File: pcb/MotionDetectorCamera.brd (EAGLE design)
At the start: 55.9 x 44.5 mm, 134 parts, among them J2 S-MOUNT-LENS-HOLDER, J3 MINI-USB-JACK, U1 LATTICE-ICE40HX4K-BG121, U10 NXP-NTB0102, U11 ON-NLAS3157, U12 ON-NLAS3157, U13 STM-STM32F730, U2 TI-TPS6280XYKAR, U22 TI-TPD4S012DRYR, U3 MICROSD-SOCKET, U4 TI-TPS6280XYKAR, U5 W989D6DBGX6I, U6 TI-TPS63805YFFR, U8 ON-AR0330CS1C12SPKA0, U9 TI-TMUX1574, X1 SITIME-SIT8021, X2 SITIME-SIT8021

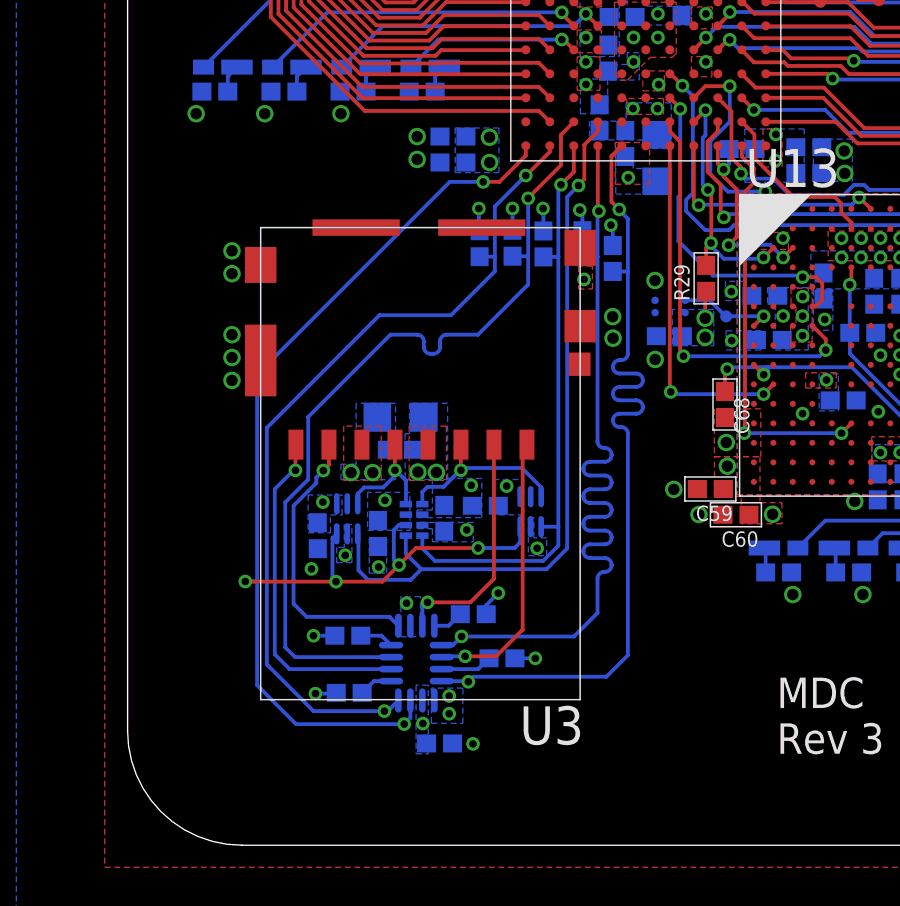
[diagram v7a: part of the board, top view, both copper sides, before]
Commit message: In process of length-matching SDIO lines
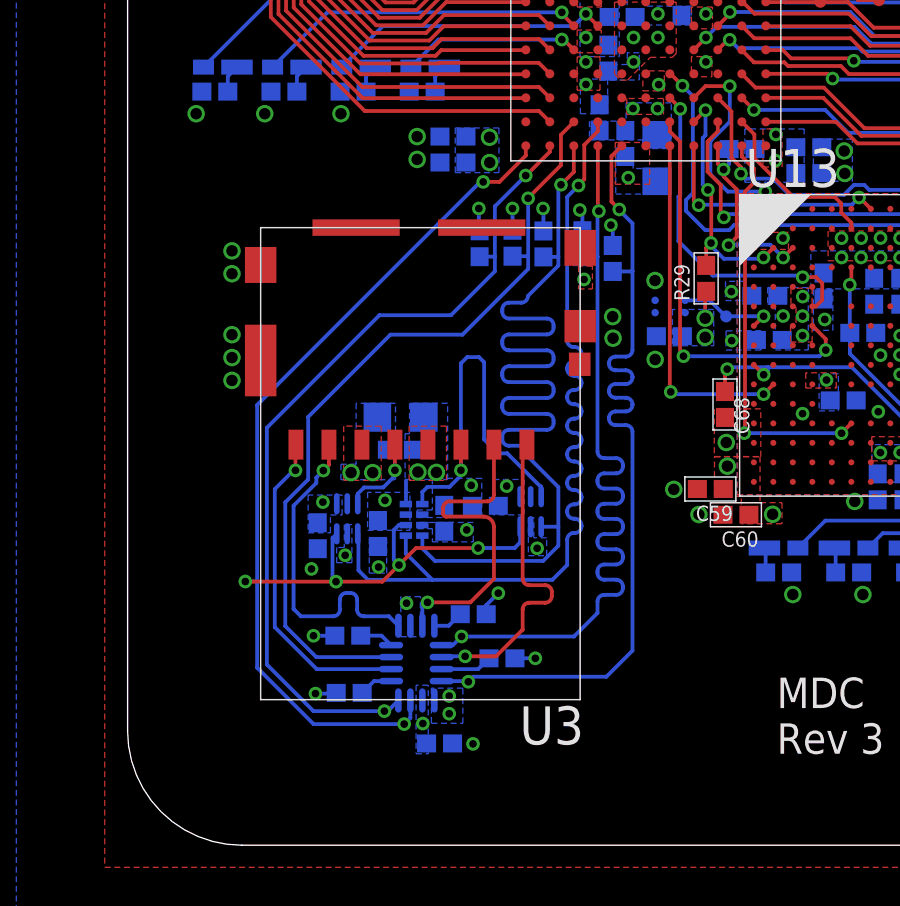
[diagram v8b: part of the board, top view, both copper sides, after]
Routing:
- net ICE_SD_CMD: track 20.0 -> 33.6 mm
- net SD_CMD: track 6.13 -> 13.3 mm
- net ICE_SD_CLK: track 24.7 -> 29.0 mm
- net SD_DAT3: track 7.86 -> 10.7 mm
- net ICE_SD_DAT1: track 28.1 -> 26.7 mm
- net SD_DAT2: track 9.30 -> 10.7 mm
- net SD_DAT0: track 9.59 -> 10.7 mm
- net ICE_SD_INIT: track 43.0 -> 42.1 mm
- net SD_DAT1: track 11.4 -> 10.9 mm
- net SD_CLK: track 4.15 -> 3.64 mm
